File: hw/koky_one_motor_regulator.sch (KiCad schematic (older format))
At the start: 15 parts, among them CON1 ISP-MLW-6, SW1 Rotary_Encoder_Switch, U1 ATMEGA328P-PU, U2 StepStick, Y1 16MHz

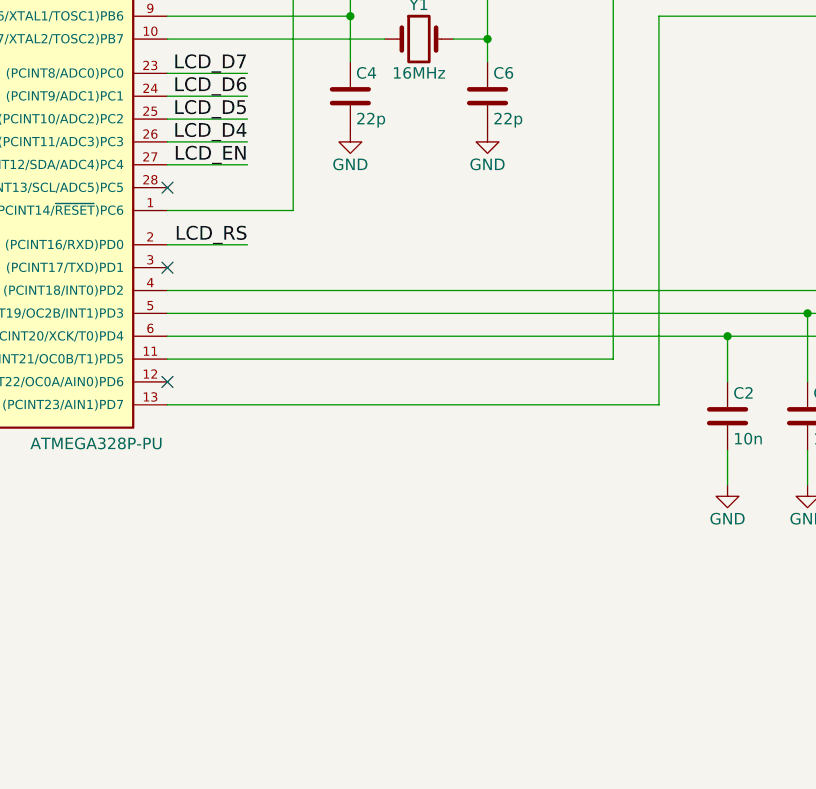
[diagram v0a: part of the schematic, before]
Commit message: add teperature measurment
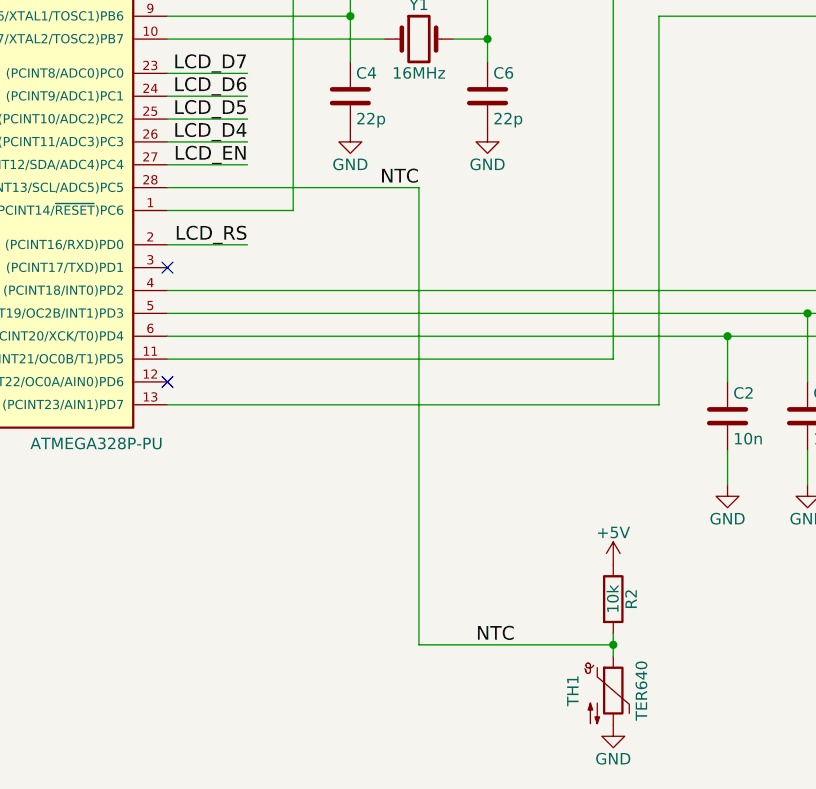
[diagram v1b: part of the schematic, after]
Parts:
- added R2: 10k, symbol R
- added TH1: TER640, symbol Thermistor_NTC
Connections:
- net +5V: now also R2.1
- net GND: now also TH1.2
- net NTC: now reaches U1.28 ((PCINT13/SCL/ADC5)PC5)
- net NTC: now also R2.2, TH1.1
- no-connect marks 3 -> 2
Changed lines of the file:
@@
 $EndComp
 $Comp
-L GND #PWR8
+L GND #PWR12
 U 1 1 5962981A
 P 8000 5800
-F 0 "#PWR8" H 8000 5550 50  0001 C CNN
+F 0 "#PWR12" H 8000 5550 50  0001 C CNN
 F 1 "GND" H 8000 5650 50  0000 C CNN
 F 2 "" H 8000 5800 50  0001 C CNN
@@
 $EndComp
 $Comp
-L GND #PWR11
+L GND #PWR17
 U 1 1 59629829
 P 9000 5800
-F 0 "#PWR11" H 9000 5550 50  0001 C CNN
+F 0 "#PWR17" H 9000 5550 50  0001 C CNN
 F 1 "GND" H 9000 5650 50  0000 C CNN
 F 2 "" H 9000 5800 50  0001 C CNN
@@
 $EndComp
 $Comp
-L GND #PWR3
+L GND #PWR9
 U 1 1 5962A1D8
 P 6950 5800
-F 0 "#PWR3" H 6950 5550 50  0001 C CNN
+F 0 "#PWR9" H 6950 5550 50  0001 C CNN
 F 1 "GND" H 6950 5650 50  0000 C CNN
 F 2 "" H 6950 5800 50  0001 C CNN
@@
 $EndComp
 $Comp
-L GND #PWR4
+L GND #PWR10
 U 1 1 5962A2F5
 P 7300 5800
-F 0 "#PWR4" H 7300 5550 50  0001 C CNN
+F 0 "#PWR10" H 7300 5550 50  0001 C CNN
 F 1 "GND" H 7300 5650 50  0000 C CNN
 F 2 "" H 7300 5800 50  0001 C CNN
@@
 $EndComp
 $Comp
-L GND #PWR6
+L GND #PWR11
 U 1 1 5962A30A
 P 7650 5800
-F 0 "#PWR6" H 7650 5550 50  0001 C CNN
+F 0 "#PWR11" H 7650 5550 50  0001 C CNN
 F 1 "GND" H 7650 5650 50  0000 C CNN
 F 2 "" H 7650 5800 50  0001 C CNN
@@
 $EndComp
 $Comp
-L GND #PWR10
+L GND #PWR5
 U 1 1 5962DEC7
 P 5900 2200
-F 0 "#PWR10" H 5900 1950 50  0001 C CNN
+F 0 "#PWR5" H 5900 1950 50  0001 C CNN
 F 1 "GND" H 5900 2050 50  0000 C CNN
 F 2 "" H 5900 2200 50  0001 C CNN
@@
 $EndComp
 $Comp
-L +5V #PWR9
+L +5V #PWR4
 U 1 1 5962DFA6
 P 5900 1600
-F 0 "#PWR9" H 5900 1450 50  0001 C CNN
+F 0 "#PWR4" H 5900 1450 50  0001 C CNN
 F 1 "+5V" H 5900 1740 50  0000 C CNN
 F 2 "" H 5900 1600 50  0001 C CNN
@@
 Connection ~ 5300 3750
 $Comp
-L GND #PWR7
+L GND #PWR6
 U 1 1 59630C28
 P 5900 4250
-F 0 "#PWR7" H 5900 4000 50  0001 C CNN
+F 0 "#PWR6" H 5900 4000 50  0001 C CNN
 F 1 "GND" H 5900 4100 50  0000 C CNN
 F 2 "" H 5900 4250 50  0001 C CNN
@@
 $EndComp
 $Comp
-L GND #PWR5
+L GND #PWR3
 U 1 1 59630CB2
 P 5300 4250
-F 0 "#PWR5" H 5300 4000 50  0001 C CNN
+F 0 "#PWR3" H 5300 4000 50  0001 C CNN
 F 1 "GND" H 5300 4100 50  0000 C CNN
 F 2 "" H 5300 4250 50  0001 C CNN
@@
 $EndComp
 $Comp
-L +5V #PWR14
+L +5V #PWR13
 U 1 1 5963155C
 P 8400 2350
-F 0 "#PWR14" H 8400 2200 50  0001 C CNN
+F 0 "#PWR13" H 8400 2200 50  0001 C CNN
 F 1 "+5V" H 8400 2490 50  0000 C CNN
 F 2 "" H 8400 2350 50  0001 C CNN
@@
 	8400 2350 8400 2450
 $Comp
-L +12V #PWR16
+L +12V #PWR15
 U 1 1 5963175D
 P 8700 2350
-F 0 "#PWR16" H 8700 2200 50  0001 C CNN
+F 0 "#PWR15" H 8700 2200 50  0001 C CNN
 F 1 "+12V" H 8700 2490 50  0000 C CNN
 F 2 "" H 8700 2350 50  0001 C CNN
@@
 	9150 2400 9100 2400
 $Comp
-L GND #PWR17
+L GND #PWR16
 U 1 1 596320C6
 P 8700 4200
-F 0 "#PWR17" H 8700 3950 50  0001 C CNN
+F 0 "#PWR16" H 8700 3950 50  0001 C CNN
 F 1 "GND" H 8700 4050 50  0000 C CNN
 F 2 "" H 8700 4200 50  0001 C CNN
@@
 $EndComp
 $Comp
-L GND #PWR15
+L GND #PWR14
 U 1 1 59632181
 P 8400 4200
-F 0 "#PWR15" H 8400 3950 50  0001 C CNN
+F 0 "#PWR14" H 8400 3950 50  0001 C CNN
 F 1 "GND" H 8400 4050 50  0000 C CNN
 F 2 "" H 8400 4200 50  0001 C CNN
@@
 	6250 2050 6250 3450
 Connection ~ 6250 2850
-NoConn ~ 4500 4500
+$Comp
+L R R2
+U 1 1 5992E6D2
+P 6450 6300
+F 0 "R2" V 6530 6300 50  0000 C CNN
+F 1 "10k" V 6450 6300 50  0000 C CNN
+F 2 "" V 6380 6300 50  0001 C CNN
+F 3 "" H 6450 6300 50  0001 C CNN
+	1    6450 6300
+	1    0    0    -1
+$EndComp
+$Comp
+L Thermistor_NTC TH1
+U 1 1 5992E78F
+P 6450 6700
+F 0 "TH1" V 6275 6700 50  0000 C CNN
+F 1 "TER640" V 6575 6700 50  0000 C CNN
+F 2 "" H 6450 6750 50  0001 C CNN
+F 3 "" H 6450 6750 50  0001 C CNN
+	1    6450 6700
+	1    0    0    -1
+$EndComp
+$Comp
+L GND #PWR8
+U 1 1 5992E8B3
+P 6450 6850
+F 0 "#PWR8" H 6450 6600 50  0001 C CNN
+F 1 "GND" H 6450 6700 50  0000 C CNN
+F 2 "" H 6450 6850 50  0001 C CNN
+F 3 "" H 6450 6850 50  0001 C CNN
+	1    6450 6850
+	1    0    0    -1
+$EndComp
+$Comp
+L +5V #PWR7
+U 1 1 5992E8E9
+P 6450 6150
+F 0 "#PWR7" H 6450 6000 50  0001 C CNN
+F 1 "+5V" H 6450 6290 50  0000 C CNN
+F 2 "" H 6450 6150 50  0001 C CNN
+F 3 "" H 6450 6150 50  0001 C CNN
+	1    6450 6150
+	1    0    0    -1
+$EndComp
+Wire Wire Line
+	6450 6550 6450 6450
+Wire Wire Line
+	5600 6500 6450 6500
+Connection ~ 6450 6500
+Wire Wire Line
+	4500 4500 5600 4500
+Wire Wire Line
+	5600 4500 5600 6500
+Text Label 5850 6500 0    60   ~ 0
+NTC
+Text Label 5600 4500 2    60   ~ 0
+NTC
 $EndSCHEMATC

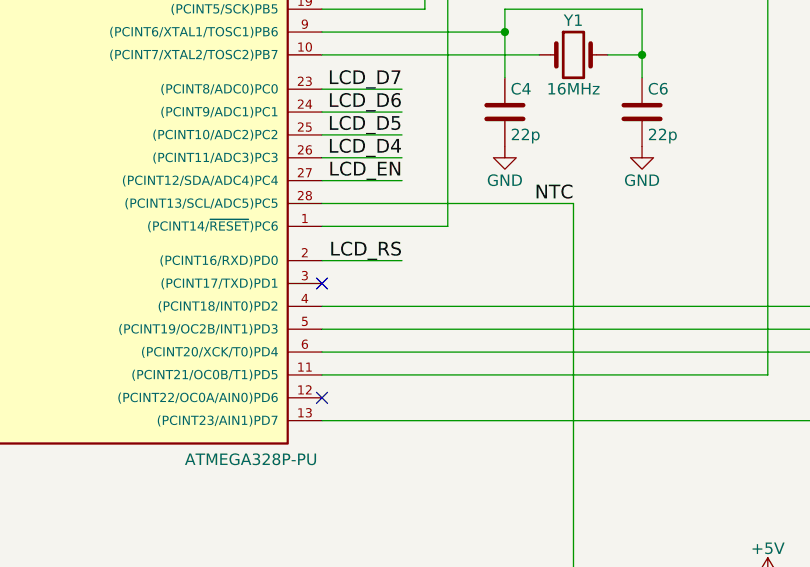
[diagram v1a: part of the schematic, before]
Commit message: add valve output
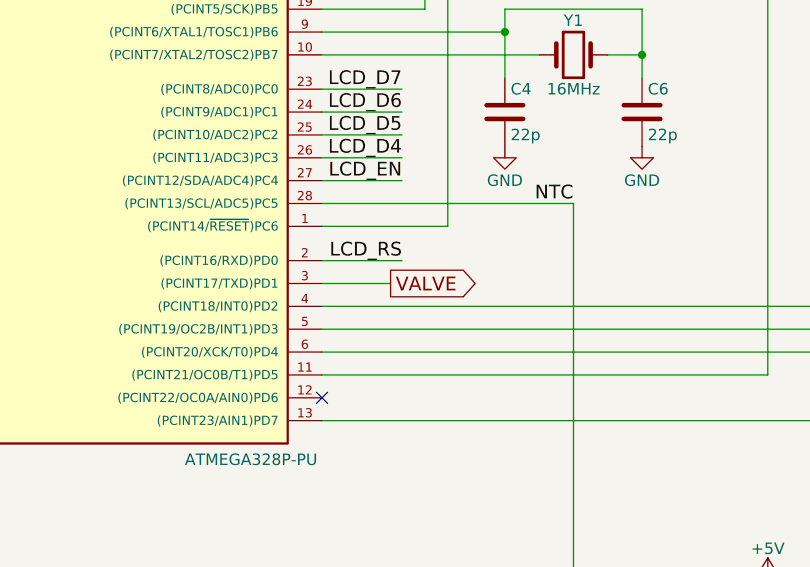
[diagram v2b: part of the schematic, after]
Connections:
- net VALVE: now reaches U1.3 ((PCINT17/TXD)PD1)
- no-connect marks 2 -> 1
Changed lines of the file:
@@
 Wire Wire Line
 	4500 3350 7800 3350
-NoConn ~ 4500 4850
 Wire Wire Line
 	4500 5450 6650 5450
@@
 Text Label 5600 4500 2    60   ~ 0
 NTC
+Text GLabel 4800 4850 2    60   Output ~ 0
+VALVE
+Wire Wire Line
+	4800 4850 4500 4850
 $EndSCHEMATC
